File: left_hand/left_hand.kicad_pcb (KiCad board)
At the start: 2 copper layers, 75 x 85 mm, 56 parts, among them J1 Conn_01x08, J2 Screw_Terminal_01x10, J3 Conn_01x02, J4 Conn_01x02, J5 8P8C_Shielded, J6 Conn_02x02_Top_Bottom, J7 Conn_01x08, J8 Conn_01x03, M1 Motor_Servo, M2 Motor_Servo, M3 Motor_Servo, M4 Motor_Servo, M5 Motor_Servo, Q1 Q_NMOS_GDS, Q2 Q_NMOS_GDS, Q3 Q_NMOS_GDS, Q4 Q_NMOS_GDS, Q5 Q_NMOS_GDS, U1 MCP23017_SP, U2 PCA9685PW, U3 PCA9615DP

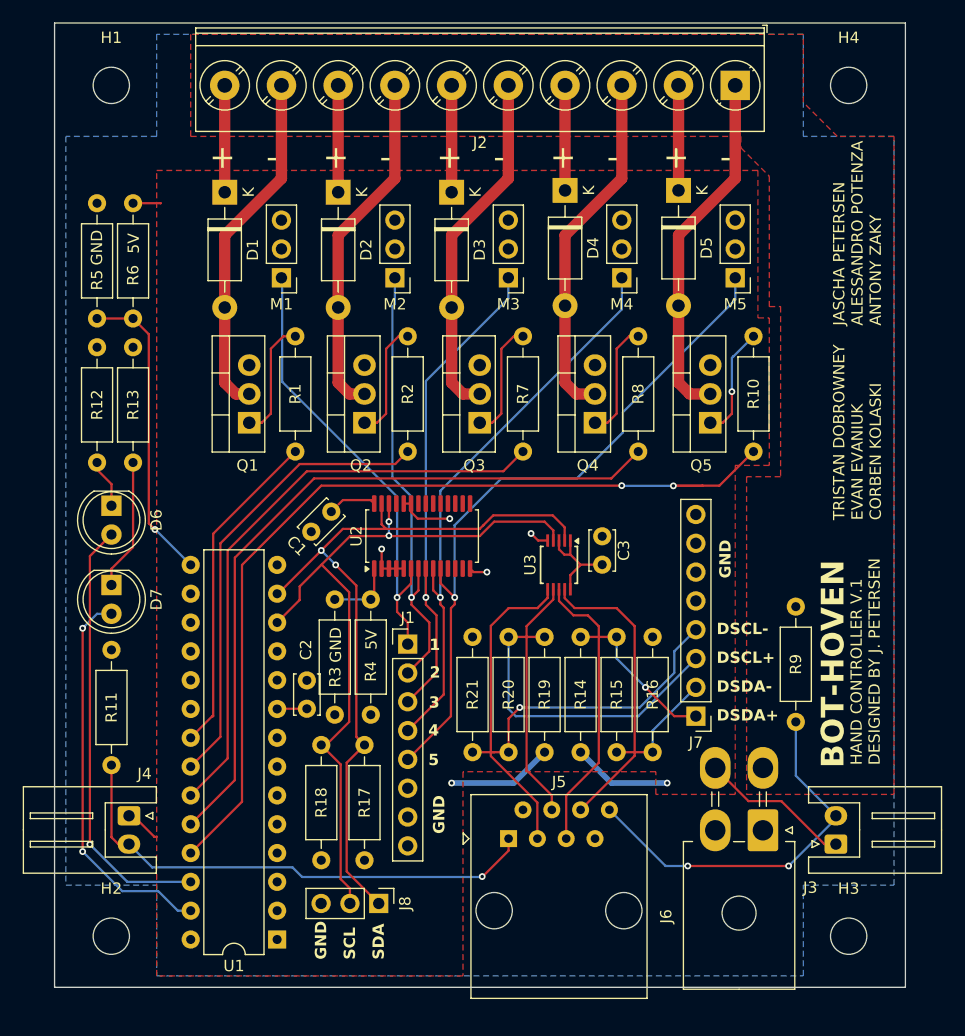
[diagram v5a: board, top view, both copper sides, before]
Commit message: As-Produced commit
This commit contains the PCBs as they were sent to the manufacturer
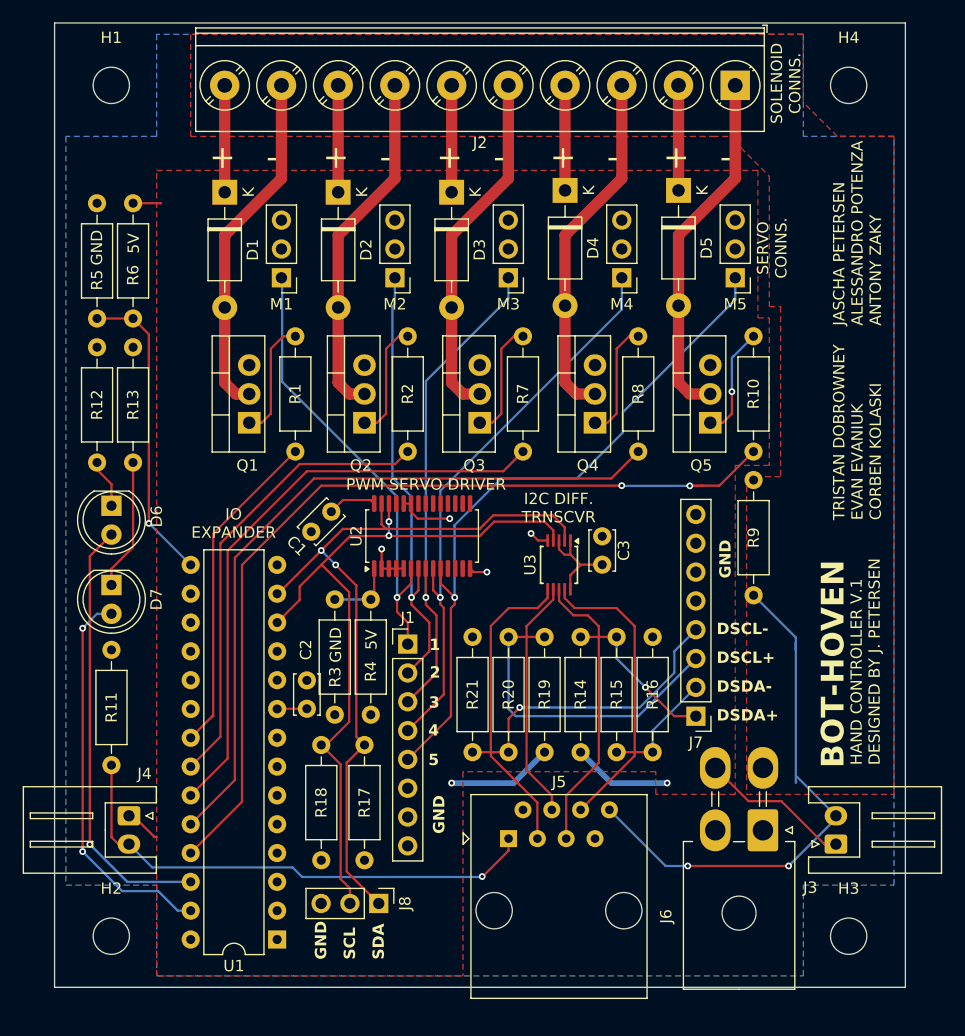
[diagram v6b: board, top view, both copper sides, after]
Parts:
- moved R9 11.8 mm to (176.6, 96.8)
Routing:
- net LIMIT_SW_R: track 34.2 -> 48.1 mm
- net Net-(U1-GPA4): track 79.1 -> 77.7 mm
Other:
- board text added: "I2C DIFF. TRNSCVR"
- board text added: "IO EXPANDER"
- board text added: "PWM SERVO DRIVER"
- board text added: "SERVO CONNS."
- board text added: "SOLENOID CONNS."
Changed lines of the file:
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@@
 		(tags "LED diameter 5.0mm 2 pins")
 		(property "Reference" "D6"
-			(at 1.27 -3.96 90)
+			(at 0.945 -3.985 90)
 			(layer "F.SilkS")
 			(effects
@@
 	(footprint "Resistor_THT:R_Axial_DIN0207_L6.3mm_D2.5mm_P10.16mm_Horizontal"
 		(layer "F.Cu")
-		(at 180.34 107.95 -90)
+		(at 176.618465 96.789608 -90)
 		(descr "Resistor, Axial_DIN0207 series, Axial, Horizontal, pin pitch=10.16mm, 0.25W = 1/4W, length*diameter=6.3*2.5mm^2, http://cdn-reichelt.de/documents/datenblatt/B400/1_4W%23YAG.pdf")
 		(tags "Resistor Axial_DIN0207 series Axial Horizontal pin pitch 10.16mm 0.25W = 1/4W length 6.3mm diameter 2.5mm")
@@
 		)
 	)
+	(gr_text "I2C DIFF.\nTRNSCVR"
+		(at 159.437437 100.640164 0)
+		(layer "F.SilkS")
+		(effects
+			(font
+				(size 1 1)
+				(thickness 0.15)
+			)
+			(justify bottom)
+		)
+	)
 	(gr_text "GND"
 		(at 139.065 139.065 90)
@@
 		)
 	)
+	(gr_text "PWM SERVO DRIVER"
+		(at 147.742791 97.761482 0)
+		(layer "F.SilkS")
+		(effects
+			(font
+				(size 1 1)
+				(thickness 0.15)
+			)
+			(justify bottom)
+		)
+	)
 	(gr_text "-"
 		(at 153.686469 69.5 0)
@@
 		)
 	)
+	(gr_text "SERVO\nCONNS."
+		(at 179.639249 76.339844 90)
+		(layer "F.SilkS")
+		(effects
+			(font
+				(size 1 1)
+				(thickness 0.15)
+			)
+			(justify bottom)
+		)
+	)
 	(gr_text "SCL"
 		(at 141.605 139.065 90)
@@
 		)
 	)
+	(gr_text "IO\nEXPANDER"
+		(at 130.780558 101.999084 0)
+		(layer "F.SilkS")
+		(effects
+			(font
+				(size 1 1)
+				(thickness 0.15)
+			)
+			(justify bottom)
+		)
+	)
 	(gr_text "JASCHA PETERSEN\nALESSANDRO POTENZA\nANTONY ZAKY"
 		(at 187.96 83.185 90)
@@
 		)
 	)
+	(gr_text "SOLENOID\nCONNS."
+		(at 180.859148 61.825574 90)
+		(layer "F.SilkS")
+		(effects
+			(font
+				(size 1 1)
+				(thickness 0.15)
+			)
+			(justify bottom)
+		)
+	)
 	(gr_text "SDA"
 		(at 144.145 139.065 90)
@@
 	)
 	(segment
-		(start 173.605 97.285)
-		(end 176.61 94.28)
+		(start 171 97.303934)
+		(end 171.018934 97.285)
 		(width 0.2)
 		(layer "F.Cu")
@@
 	)
 	(segment
-		(start 169.545 97.303934)
-		(end 169.563934 97.285)
+		(start 171.018934 97.285)
+		(end 173.605 97.285)
 		(width 0.2)
 		(layer "F.Cu")
@@
 	)
 	(segment
-		(start 169.563934 97.285)
-		(end 173.605 97.285)
+		(start 171 97.303934)
+		(end 172.123649 97.303934)
 		(width 0.2)
 		(layer "F.Cu")
@@
 	)
 	(segment
-		(start 138.51 97.285)
-		(end 131.525 104.27)
+		(start 173.605 97.285)
+		(end 176.61 94.28)
 		(width 0.2)
 		(layer "F.Cu")
@@
 	)
 	(segment
-		(start 131.525 125.145)
-		(end 127 129.67)
+		(start 138.51 97.285)
+		(end 131.525 104.27)
 		(width 0.2)
 		(layer "F.Cu")
@@
 	)
 	(segment
-		(start 172.142583 97.285)
-		(end 172.123649 97.303934)
+		(start 172.123649 97.303934)
+		(end 172.142583 97.285)
 		(width 0.2)
 		(layer "F.Cu")
@@
 	)
 	(segment
-		(start 172.123649 97.303934)
-		(end 169.545 97.303934)
+		(start 131.525 125.145)
+		(end 127 129.67)
 		(width 0.2)
 		(layer "F.Cu")
@@
 	)
 	(via
-		(at 169.545 97.303934)
+		(at 171 97.303934)
 		(size 0.6)
 		(drill 0.3)
@@
 	)
 	(segment
-		(start 165 97.285)
+		(start 171 97.303934)
 		(end 165.018934 97.303934)
 		(width 0.2)
@@
 	(segment
 		(start 165.018934 97.303934)
-		(end 169.545 97.303934)
+		(end 165 97.285)
 		(width 0.2)
 		(layer "B.Cu")
@@
 	)
 	(segment
-		(start 123.846513 101.147295)
-		(end 123.308554 100.609336)
-		(width 0.2)
-		(layer "F.Cu")
-		(net 44)
-	)
-	(segment
 		(start 118.745 82.55)
 		(end 121.92 82.55)
@@
 	)
 	(via
-		(at 123.846513 101.147295)
+		(at 123.308554 100.609336)
 		(size 0.6)
 		(drill 0.3)
@@
 	)
 	(segment
-		(start 127 104.27)
-		(end 123.877295 101.147295)
+		(start 123.308554 100.609336)
+		(end 123.339336 100.609336)
 		(width 0.2)
 		(layer "B.Cu")
@@
 	)
 	(segment
-		(start 123.877295 101.147295)
-		(end 123.846513 101.147295)
+		(start 123.339336 100.609336)
+		(end 127 104.27)
 		(width 0.2)
 		(layer "B.Cu")
@@
 	)
 	(segment
+		(start 180.34 111.125)
+		(end 180.34 111.76)
+		(width 0.2)
+		(layer "B.Cu")
+		(net 61)
+	)
+	(segment
 		(start 168.86 130.81)
 		(end 163.91 125.86)
@@
 	)
 	(segment
+		(start 180.34 111.125)
+		(end 180.34 110.671143)
+		(width 0.2)
+		(layer "B.Cu")
+		(net 61)
+	)
+	(segment
 		(start 183.875 126.385)
-		(end 180.34 122.85)
+		(end 184.13 126.385)
 		(width 0.2)
 		(layer "B.Cu")
@@
 	)
 	(segment
-		(start 180.34 122.85)
-		(end 180.34 118.11)
+		(start 184.13 126.385)
+		(end 184.15 126.365)
 		(width 0.2)
 		(layer "B.Cu")
@@
 	(segment
 		(start 183.875 126.385)
-		(end 184.13 126.385)
+		(end 180.34 122.85)
 		(width 0.2)
 		(layer "B.Cu")
@@
 	)
 	(segment
-		(start 184.13 126.385)
-		(end 184.15 126.365)
+		(start 180.34 110.671143)
+		(end 176.618465 106.949608)
+		(width 0.2)
+		(layer "B.Cu")
+		(net 61)
+	)
+	(segment
+		(start 180.34 123.485)
+		(end 180.34 111.125)
 		(width 0.2)
 		(layer "B.Cu")
